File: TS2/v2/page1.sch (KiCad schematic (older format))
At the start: 24 parts, among them SW1 RESET, U1 555, U2 8 MHz, U3 74LS00, U4 74LS06, U5 74LS04, U6 68000

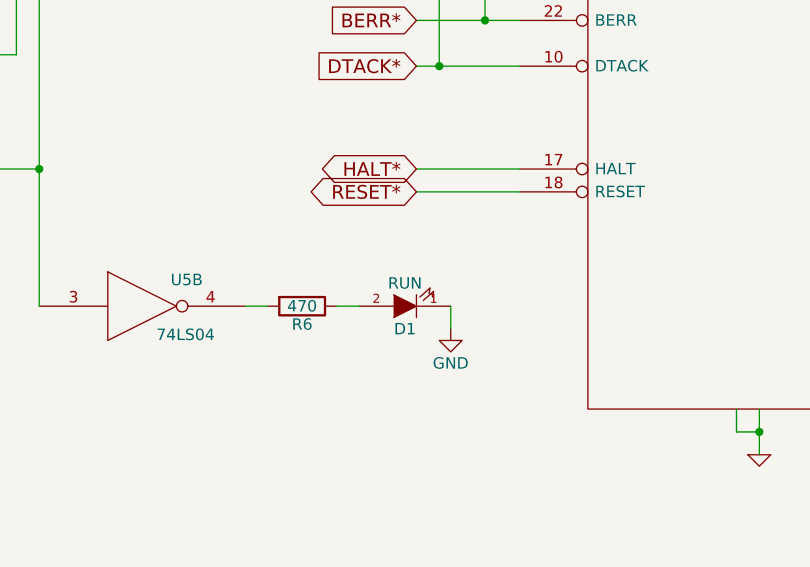
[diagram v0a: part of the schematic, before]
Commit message: Rename LED.
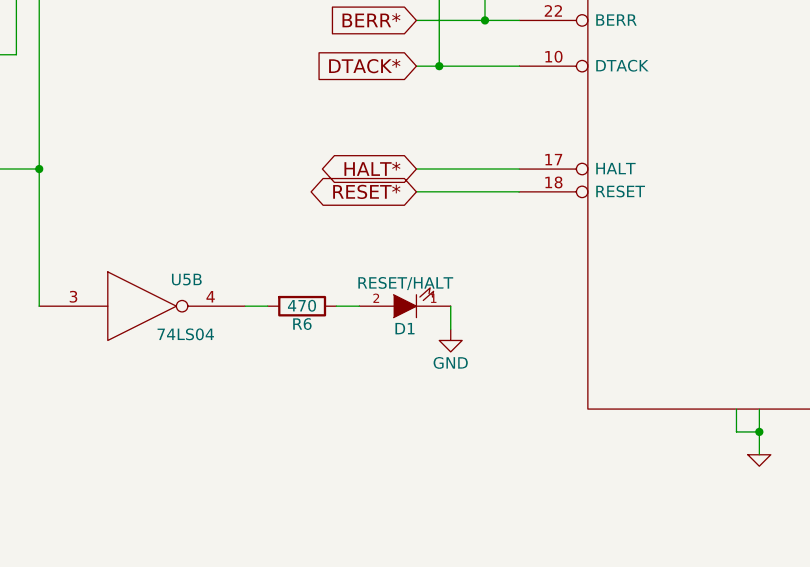
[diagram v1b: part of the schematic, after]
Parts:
- D1: value RUN -> RESET/HALT
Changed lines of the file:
@@
 P 7400 5500
 F 0 "D1" H 7400 5600 50  0000 C CNN
-F 1 "RUN" H 7400 5400 50  0000 C CNN
+F 1 "RESET/HALT" H 7400 5400 50  0000 C CNN
 F 2 "" H 7400 5500 50  0000 C CNN
 F 3 "" H 7400 5500 50  0000 C CNN

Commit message: Minor tweaks
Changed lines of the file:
@@
 $EndComp
 $Comp
-L VCC #PWR09
+L VCC #PWR011
 U 1 1 57B65815
 P 8950 1250
-F 0 "#PWR09" H 8950 1350 30  0001 C CNN
+F 0 "#PWR011" H 8950 1350 30  0001 C CNN
 F 1 "VCC" H 8950 1350 30  0000 C CNN
 F 2 "" H 8950 1250 60  0000 C CNN
@@
 $EndComp
 $Comp
-L GND-RESCUE-ts2 #PWR010
+L GND-RESCUE-ts2 #PWR012
 U 1 1 57B659E4
 P 8950 6150
-F 0 "#PWR010" H 8950 6150 30  0001 C CNN
+F 0 "#PWR012" H 8950 6150 30  0001 C CNN
 F 1 "GND" H 8950 6080 30  0001 C CNN
 F 2 "" H 8950 6150 60  0000 C CNN
@@
 $EndComp
 $Comp
-L VCC #PWR011
+L VCC #PWR013
 U 1 1 57B65F7F
 P 7500 800
-F 0 "#PWR011" H 7500 900 30  0001 C CNN
+F 0 "#PWR013" H 7500 900 30  0001 C CNN
 F 1 "VCC" H 7500 900 30  0000 C CNN
 F 2 "" H 7500 800 60  0000 C CNN
@@
 NoConn ~ 3400 6050
 $Comp
-L GND-RESCUE-ts2 #PWR012
+L GND-RESCUE-ts2 #PWR014
 U 1 1 57B66C0C
 P 2150 6600
-F 0 "#PWR012" H 2150 6600 30  0001 C CNN
+F 0 "#PWR014" H 2150 6600 30  0001 C CNN
 F 1 "GND" H 2150 6530 30  0001 C CNN
 F 2 "" H 2150 6600 60  0000 C CNN
@@
 $EndComp
 $Comp
-L VCC #PWR013
+L VCC #PWR015
 U 1 1 57B66C1B
 P 2150 5900
-F 0 "#PWR013" H 2150 6000 30  0001 C CNN
+F 0 "#PWR015" H 2150 6000 30  0001 C CNN
 F 1 "VCC" H 2150 6000 30  0000 C CNN
 F 2 "" H 2150 5900 60  0000 C CNN
@@
 $EndComp
 $Comp
-L GND-RESCUE-ts2 #PWR014
+L GND-RESCUE-ts2 #PWR016
 U 1 1 57B69495
 P 800 4700
-F 0 "#PWR014" H 800 4700 30  0001 C CNN
+F 0 "#PWR016" H 800 4700 30  0001 C CNN
 F 1 "GND" H 800 4630 30  0001 C CNN
 F 2 "" H 800 4700 60  0000 C CNN
@@
 $EndComp
 $Comp
-L VCC #PWR015
+L VCC #PWR017
 U 1 1 57B69B8D
 P 1900 3100
-F 0 "#PWR015" H 1900 3200 30  0001 C CNN
+F 0 "#PWR017" H 1900 3200 30  0001 C CNN
 F 1 "VCC" H 1900 3200 30  0000 C CNN
 F 2 "" H 1900 3100 60  0000 C CNN
@@
 $EndComp
 $Comp
-L VCC #PWR016
+L VCC #PWR018
 U 1 1 57B6A9BF
 P 1650 750
-F 0 "#PWR016" H 1650 850 30  0001 C CNN
+F 0 "#PWR018" H 1650 850 30  0001 C CNN
 F 1 "VCC" H 1650 850 30  0000 C CNN
 F 2 "" H 1650 750 60  0000 C CNN
@@
 $EndComp
 $Comp
-L GND-RESCUE-ts2 #PWR017
+L GND-RESCUE-ts2 #PWR019
 U 1 1 57B6AB1C
 P 1150 2850
-F 0 "#PWR017" H 1150 2850 30  0001 C CNN
+F 0 "#PWR019" H 1150 2850 30  0001 C CNN
 F 1 "GND" H 1150 2780 30  0001 C CNN
 F 2 "" H 1150 2850 60  0000 C CNN
@@
 $EndComp
 $Comp
-L VCC #PWR018
+L VCC #PWR020
 U 1 1 57BE8ECB
 P 7550 3750
-F 0 "#PWR018" H 7550 3600 50  0001 C CNN
+F 0 "#PWR020" H 7550 3600 50  0001 C CNN
 F 1 "VCC" H 7550 3900 50  0000 C CNN
 F 2 "" H 7550 3750 50  0000 C CNN
@@
 $EndComp
 $Comp
-L VCC #PWR019
+L VCC #PWR021
 U 1 1 57BE8F17
 P 7300 2700
-F 0 "#PWR019" H 7300 2550 50  0001 C CNN
+F 0 "#PWR021" H 7300 2550 50  0001 C CNN
 F 1 "VCC" H 7300 2850 50  0000 C CNN
 F 2 "" H 7300 2700 50  0000 C CNN
@@
 	7600 5500 7600 5600
 $Comp
-L GND #PWR020
+L GND #PWR022
 U 1 1 57CB0CEF
 P 7600 5600
-F 0 "#PWR020" H 7600 5350 50  0001 C CNN
+F 0 "#PWR022" H 7600 5350 50  0001 C CNN
 F 1 "GND" H 7600 5450 50  0000 C CNN
 F 2 "" H 7600 5600 50  0000 C CNN
@@
 	6900 2400 6900 2100
 $Comp
-L VCC #PWR021
+L VCC #PWR023
 U 1 1 57CB713B
 P 6900 1800
-F 0 "#PWR021" H 6900 1650 50  0001 C CNN
+F 0 "#PWR023" H 6900 1650 50  0001 C CNN
 F 1 "VCC" H 6900 1950 50  0000 C CNN
 F 2 "" H 6900 1800 50  0000 C CNN
@@
 $EndComp
 $Comp
-L VCC #PWR022
+L VCC #PWR024
 U 1 1 57CB7189
 P 7100 1800
-F 0 "#PWR022" H 7100 1650 50  0001 C CNN
+F 0 "#PWR024" H 7100 1650 50  0001 C CNN
 F 1 "VCC" H 7100 1950 50  0000 C CNN
 F 2 "" H 7100 1800 50  0000 C CNN
@@
 	3150 2050 3250 2050
 Connection ~ 3250 2050
+Connection ~ 1900 3300
 $EndSCHEMATC

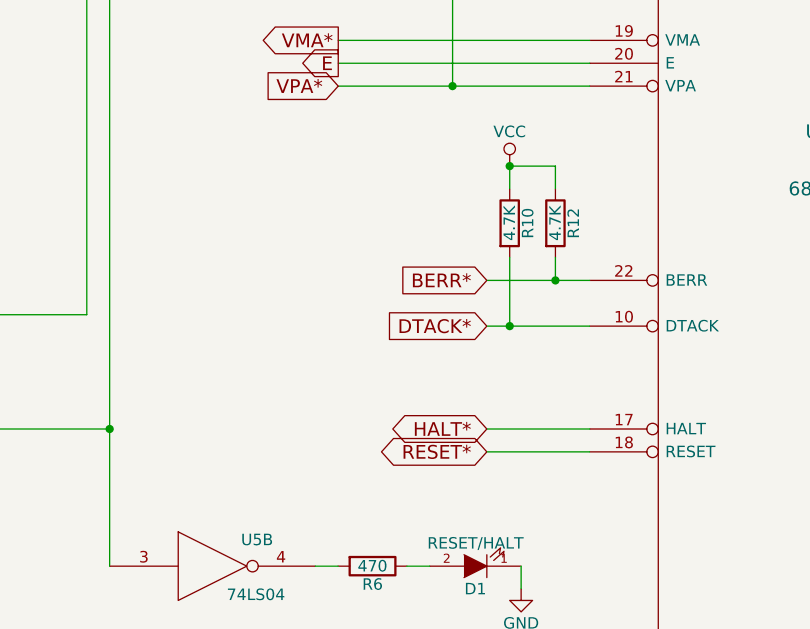
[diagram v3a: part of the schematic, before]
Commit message: Add missing pullups on HALT* and RESET*.
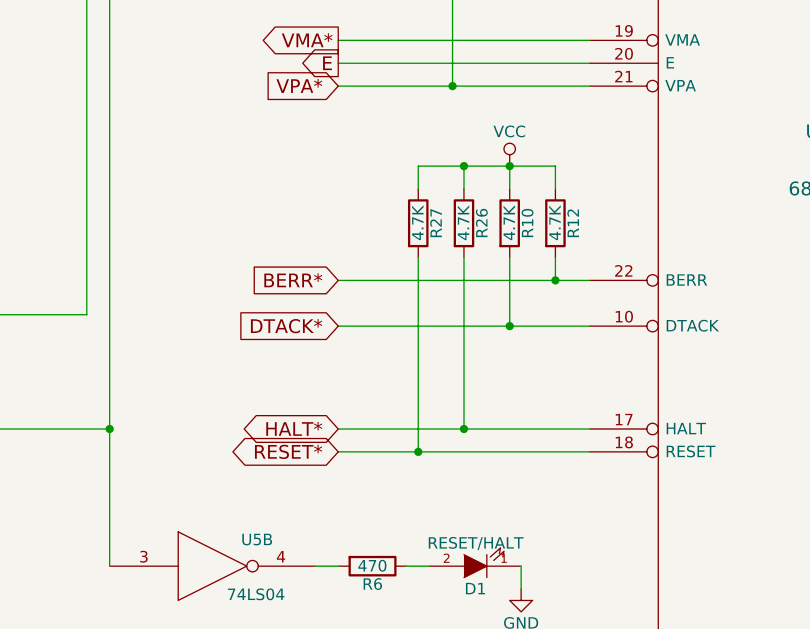
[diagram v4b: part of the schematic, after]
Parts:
- added R26, R27: 4.7K, symbol R
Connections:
- net HALT*: now also R26.2
- net RESET*: now also R27.2
- net VCC: now also R26.1, R27.1
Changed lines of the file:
@@
 Text GLabel 5900 2650 2    60   Output ~ 0
 HALT*
-Text GLabel 7450 4900 0    60   BiDi ~ 0
+Text GLabel 6800 4900 0    60   BiDi ~ 0
 HALT*
-Text GLabel 7450 5000 0    60   BiDi ~ 0
+Text GLabel 6800 5000 0    60   BiDi ~ 0
 RESET*
 $Comp
@@
 Connection ~ 5800 2650
 Wire Wire Line
-	7900 4900 7450 4900
-Wire Wire Line
-	7900 5000 7450 5000
-Wire Wire Line
-	7450 4450 7900 4450
-Wire Wire Line
-	7450 4250 7900 4250
+	6800 4900 7900 4900
+Wire Wire Line
+	6800 5000 7900 5000
+Wire Wire Line
+	6800 4450 7900 4450
+Wire Wire Line
+	6800 4250 7900 4250
 Wire Wire Line
 	7750 4250 7750 4150
@@
 	7550 4150 7550 4450
 Wire Wire Line
-	7750 3850 7750 3750
+	7750 3750 7750 3850
 Wire Wire Line
 	7550 3850 7550 3750
@@
 	6800 3400 7900 3400
 Wire Wire Line
-	7550 3750 7750 3750
+	7150 3750 7750 3750
 Wire Wire Line
 	9900 1800 10000 1800
@@
 Wire Wire Line
 	6800 3300 7900 3300
-Text GLabel 7450 4250 0    60   Input ~ 0
+Text GLabel 6800 4250 0    60   Input ~ 0
 BERR*
 Connection ~ 7750 4250
-Text GLabel 7450 4450 0    60   Input ~ 0
+Text GLabel 6800 4450 0    60   Input ~ 0
 DTACK*
 Connection ~ 7550 4450
@@
 Connection ~ 3250 2050
 Connection ~ 1900 3300
+$Comp
+L R R26
+U 1 1 58362FB7
+P 7350 4000
+F 0 "R26" V 7430 4000 50  0000 C CNN
+F 1 "4.7K" V 7350 4000 50  0000 C CNN
+F 2 "" V 7280 4000 50  0000 C CNN
+F 3 "" H 7350 4000 50  0000 C CNN
+	1    7350 4000
+	1    0    0    -1
+$EndComp
+$Comp
+L R R27
+U 1 1 5836302F
+P 7150 4000
+F 0 "R27" V 7230 4000 50  0000 C CNN
+F 1 "4.7K" V 7150 4000 50  0000 C CNN
+F 2 "" V 7080 4000 50  0000 C CNN
+F 3 "" H 7150 4000 50  0000 C CNN
+	1    7150 4000
+	1    0    0    -1
+$EndComp
+Wire Wire Line
+	7150 3750 7150 3850
+Wire Wire Line
+	7350 3850 7350 3750
+Connection ~ 7350 3750
+Wire Wire Line
+	7350 4150 7350 4900
+Connection ~ 7350 4900
+Wire Wire Line
+	7150 4150 7150 5000
+Connection ~ 7150 5000
 $EndSCHEMATC
